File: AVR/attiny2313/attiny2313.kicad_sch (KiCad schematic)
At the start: 9 parts

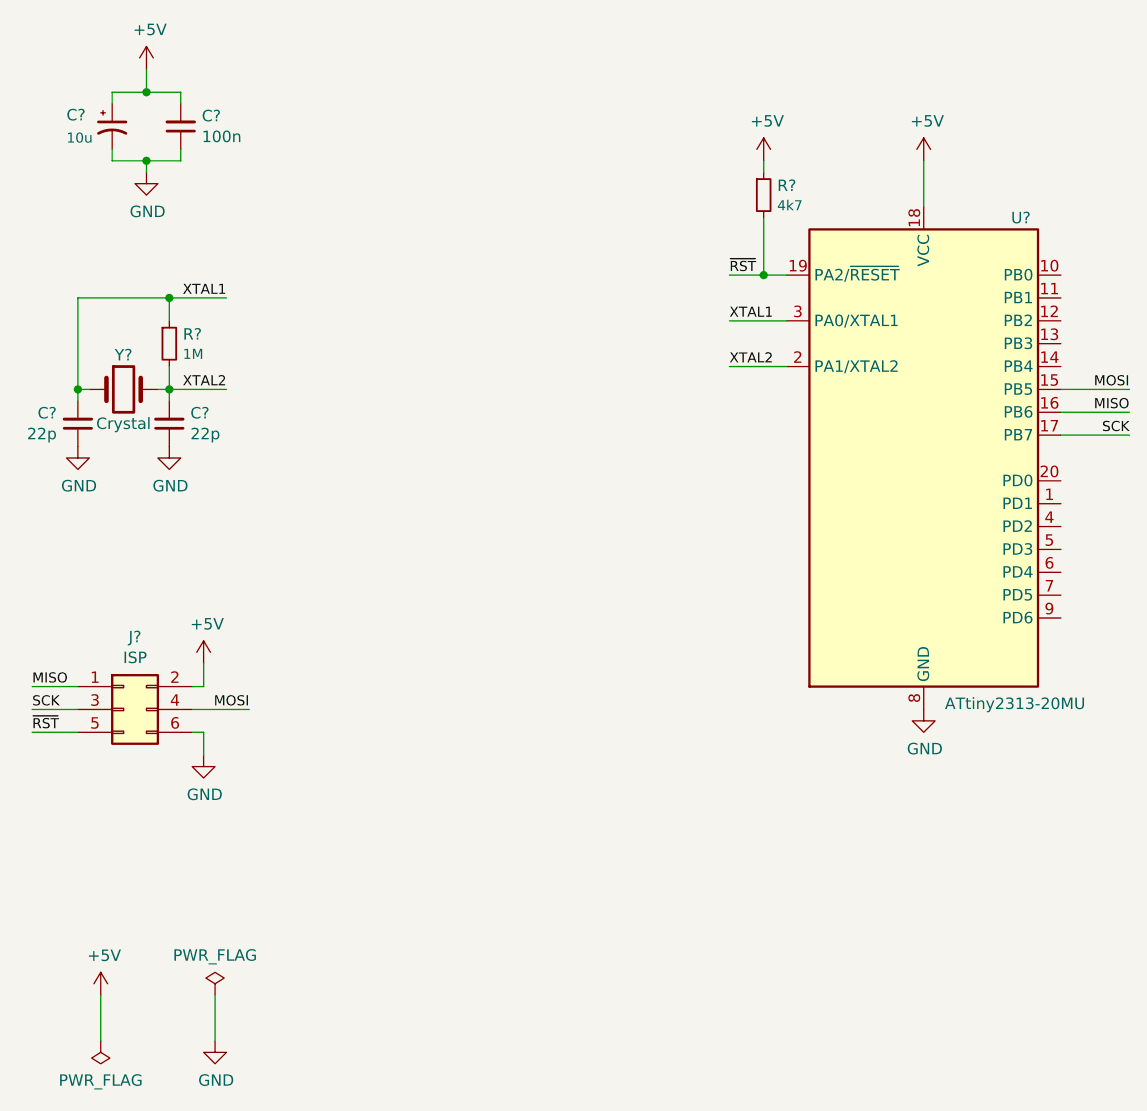
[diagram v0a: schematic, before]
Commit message: Fix grid alignment and update to KiCad 9
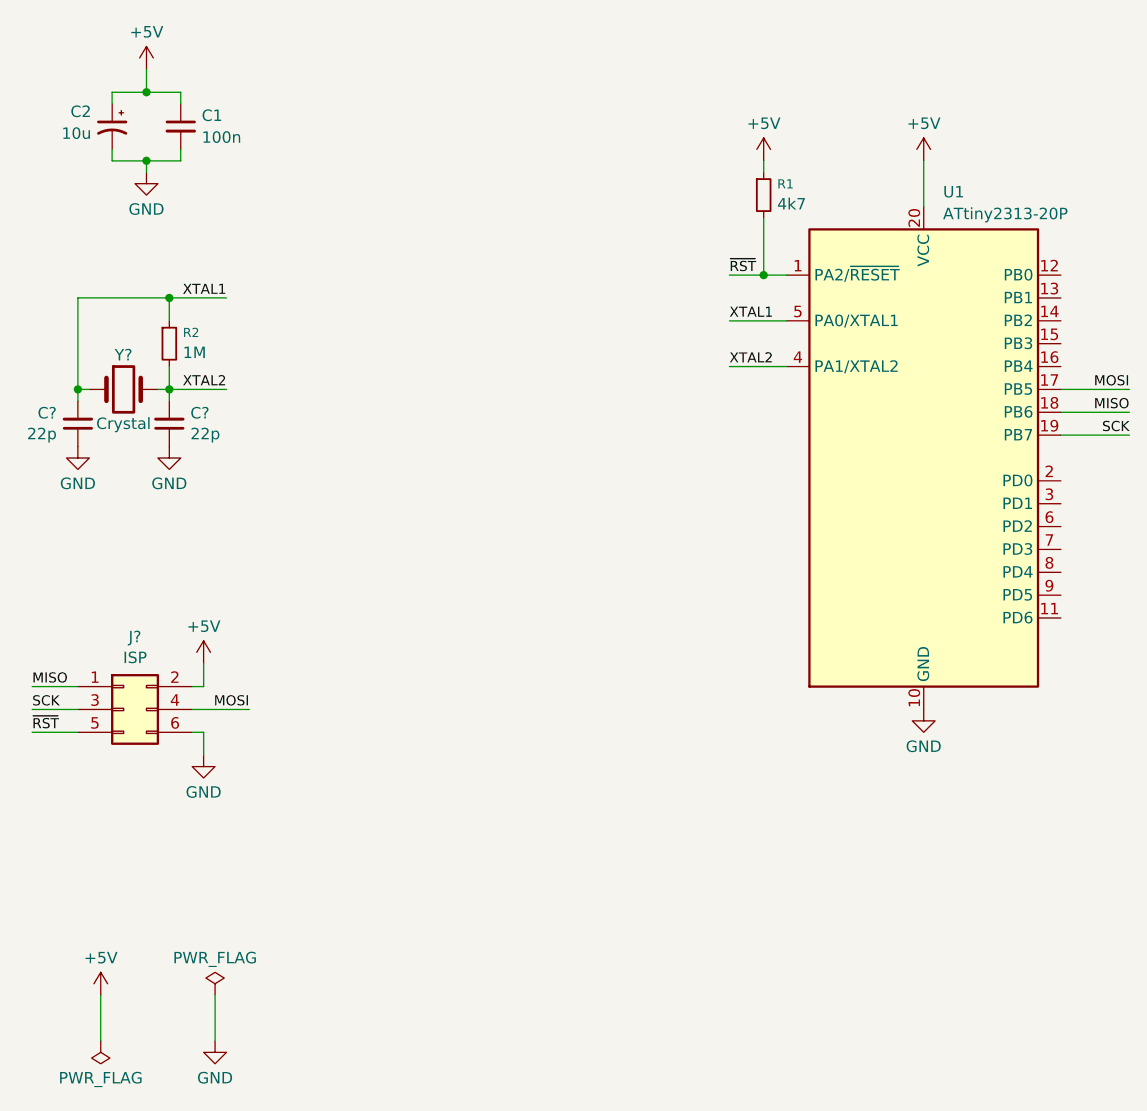
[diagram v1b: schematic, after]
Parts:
- removed C?: 10u, symbol Device:CP1_Small
- removed C?: 100n, symbol Device:C_Small
- removed R?: 1M, symbol Device:R_Small
- removed R?: 4k7, symbol Device:R_Small
- removed U?: ATtiny2313-20MU, Package_DFN_QFN:QFN-20-1EP_4x4mm_P0.5mm_EP2.25x2.25mm, symbol attiny2313-rescue:ATtiny2313-20MU-MCU_Microchip_ATtiny
- added C1: 100n, symbol Device:C_Small
- added C2: 10u, symbol Device:C_Polarized_Small_US
- added R1: 4k7, symbol Device:R_Small
- added R2: 1M, symbol Device:R_Small
- added U1: ATtiny2313-20P, Package_DIP:DIP-20_W7.62mm, symbol MCU_Microchip_ATtiny:ATtiny2313-20P
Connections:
- net +5V: now also C1.1, C2.1, R1.1, U1.20 (VCC)
- net GND: now also C1.2, C2.2, U1.10 (GND)
- net MISO: now also U1.18 (PB6)
- net MOSI: now also U1.17 (PB5)
- net SCK: now also U1.19 (PB7)
- net XTAL1: now also R2.1, U1.5 (PA0/XTAL1)
- net XTAL2: now also R2.2, U1.4 (PA1/XTAL2)
- net ~{RST}: now also R1.2, U1.1 (PA2/~{RESET})
